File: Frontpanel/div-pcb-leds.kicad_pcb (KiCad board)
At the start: 2 copper layers, 20 x 128.5 mm, 0 parts

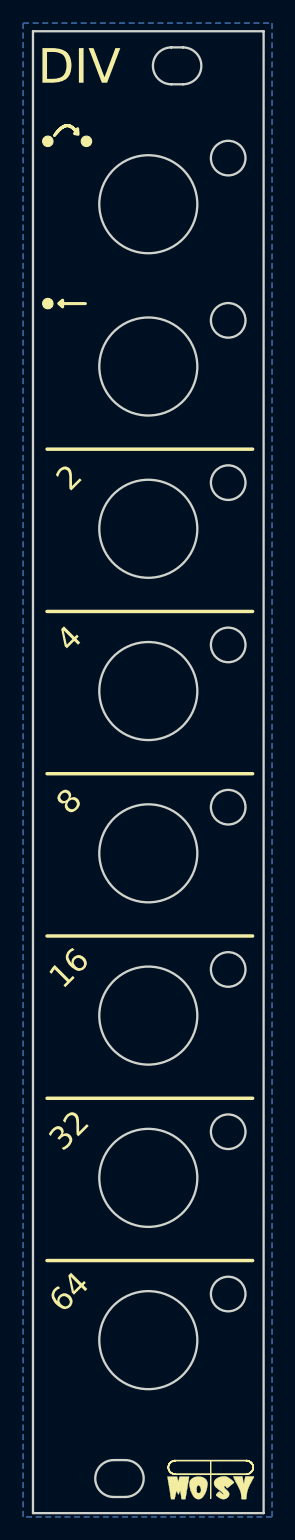
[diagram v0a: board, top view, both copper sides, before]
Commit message: :hammer: Extend frontpanel copper layer to front and back side
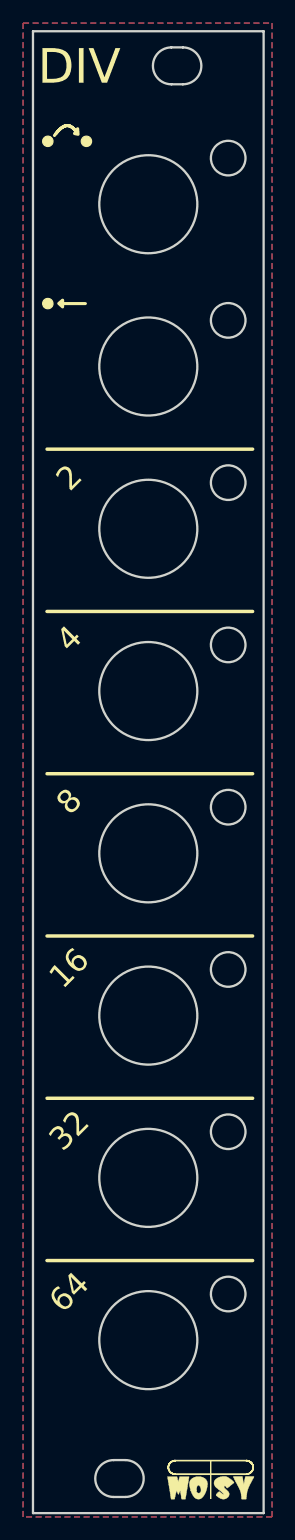
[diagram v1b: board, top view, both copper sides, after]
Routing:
- added copper zone on F.Cu, net (none)
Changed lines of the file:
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@@
     (effects (font (size 2 2) (thickness 0.2)) (justify bottom))
   )
-  (zone (net 0) (net_name "") (layer "B.Cu") (hatch edge 0.5)
+  (zone (net 0) (net_name "") (layers "F&B.Cu") (hatch edge 0.5)
     (connect_pads (clearance 0.5))
     (min_thickness 0.25) (filled_areas_thickness no)

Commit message: :memo: Change frontpanel release to v1.1
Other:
- board text added: "v1.1"
- board text removed: "v1"
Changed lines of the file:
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@@
   (title_block
     (title "moPsy DIV (LEDs)")
-    (date "2023-04-07")
-    (rev "v1")
+    (date "2023-05-17")
+    (rev "v1.1")
   )
   (layers
@@
     (effects (font (size 2 2) (thickness 0.2)) (justify left bottom mirror))
   )
-  (gr_text "v1" (at 108.839 119.38 90) (layer "B.SilkS")
+  (gr_text "v1.1" (at 108.839 119.38 90) (layer "B.SilkS")
     (effects (font (size 2 2) (thickness 0.2)) (justify left bottom mirror))
   )
